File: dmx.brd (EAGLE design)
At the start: 56.7 x 13.8 mm, 17 parts, among them IC7 FT232RL, IC8 MAX487, X7 USB-SMD-NS

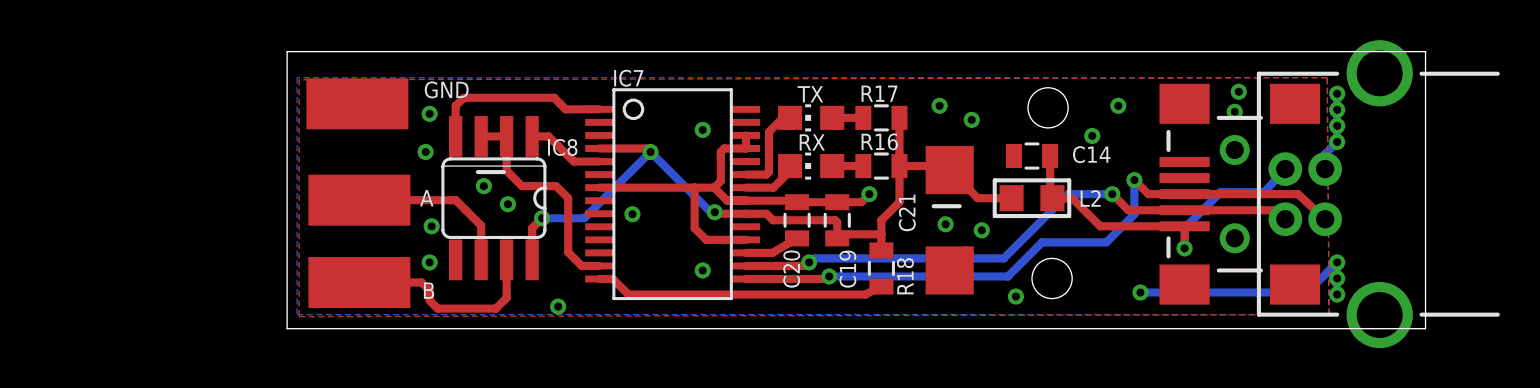
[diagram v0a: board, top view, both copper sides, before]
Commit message: proper termination
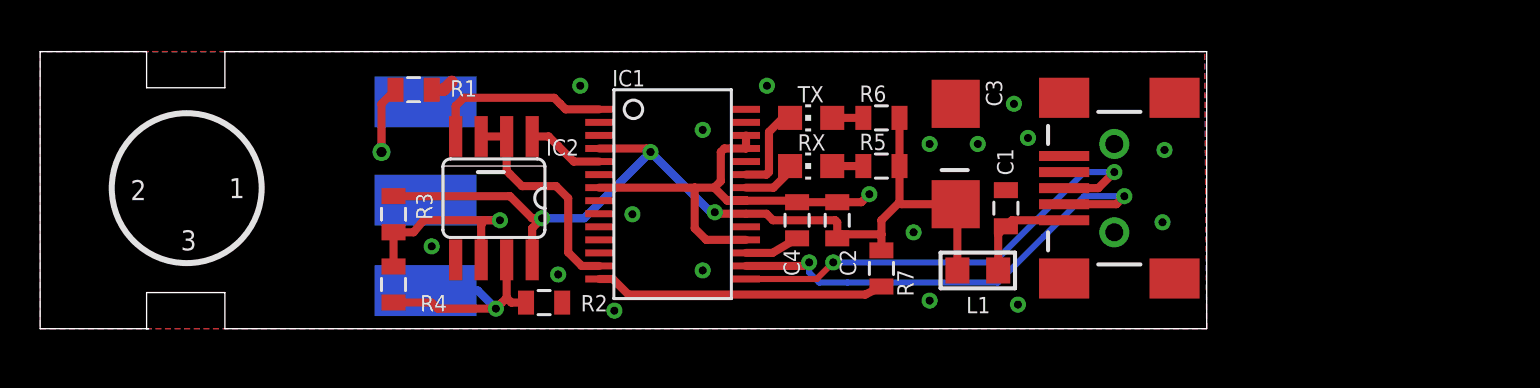
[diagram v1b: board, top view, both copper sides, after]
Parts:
- removed C14: 10nF, SparkFun:0805
- removed C21: 4.7µF, resistor:SMC_C
- removed JP1: USB-B, SparkFun-Connectors:USB-B-PTH
- removed L2: BEAD, rc-master-smd:L0805
- added C1: 10nF, SparkFun:0805
- added C3: 4.7µF, resistor:SMC_C
- added L1: BEAD, rc-master-smd:L0805
- added R1: 27R, SparkFun:0805
- added R2, R3: 680R, SparkFun:0805
- added R4: 120R, SparkFun:0805
- moved X7 6.01 mm to (35.6, -71.2)
- moved GND 3.40 mm to (1.30, -66.9), flipped to the bottom
- moved B 3.32 mm to (1.30, -76.3), flipped to the bottom
- moved A 3.30 mm to (1.30, -71.8), flipped to the bottom
- renumbered C19 to C2, C20 to C4, IC7 to IC1, IC8 to IC2, R16 to R5, R17 to R6, R18 to R7
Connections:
- new net N$2: GND.1, R1.2
- net +USB_SIEVED: now also C3.+, L1.2, R3.2; no longer C21.+, L2.2
- net GND_USB: now also C1.2, C3.-, R1.1, R2.1; no longer C14.2, C21.-, GND.1, JP1.GND
- net N$24: no longer JP1.D+
- net N$30: now also C1.1, L1.1; no longer C14.1, JP1.VBUS, L2.1
- net N$5: now also R2.2, R4.2
- net N$6: now also R3.1, R4.1
- net N$7: no longer JP1.D-
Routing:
- net GND_USB: track 40.6 -> 24.7 mm, vias 28 -> 18
- net N$30: track 18.4 -> 5.38 mm, vias 1 -> 0
- net N$24: track 32.7 -> 23.4 mm
- net N$2: track 0.00 -> 7.39 mm, vias 0 -> 1
- net +USB_SIEVED: track 40.3 -> 46.7 mm
- net N$6: track 8.30 -> 13.5 mm, vias 0 -> 1
- net N$7: track 28.8 -> 24.5 mm
- net N$5: track 10.3 -> 13.2 mm, vias 0 -> 1
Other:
- board size 56.7 x 13.8 mm -> 58.1 x 13.8 mm
- board text added: "1"
- board text added: "2"
- board text added: "3"
